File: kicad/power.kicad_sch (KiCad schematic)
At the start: 31 parts, among them J101 24VDC IN, U101 LMR16006YQ5, U102 AMS1117-3.3

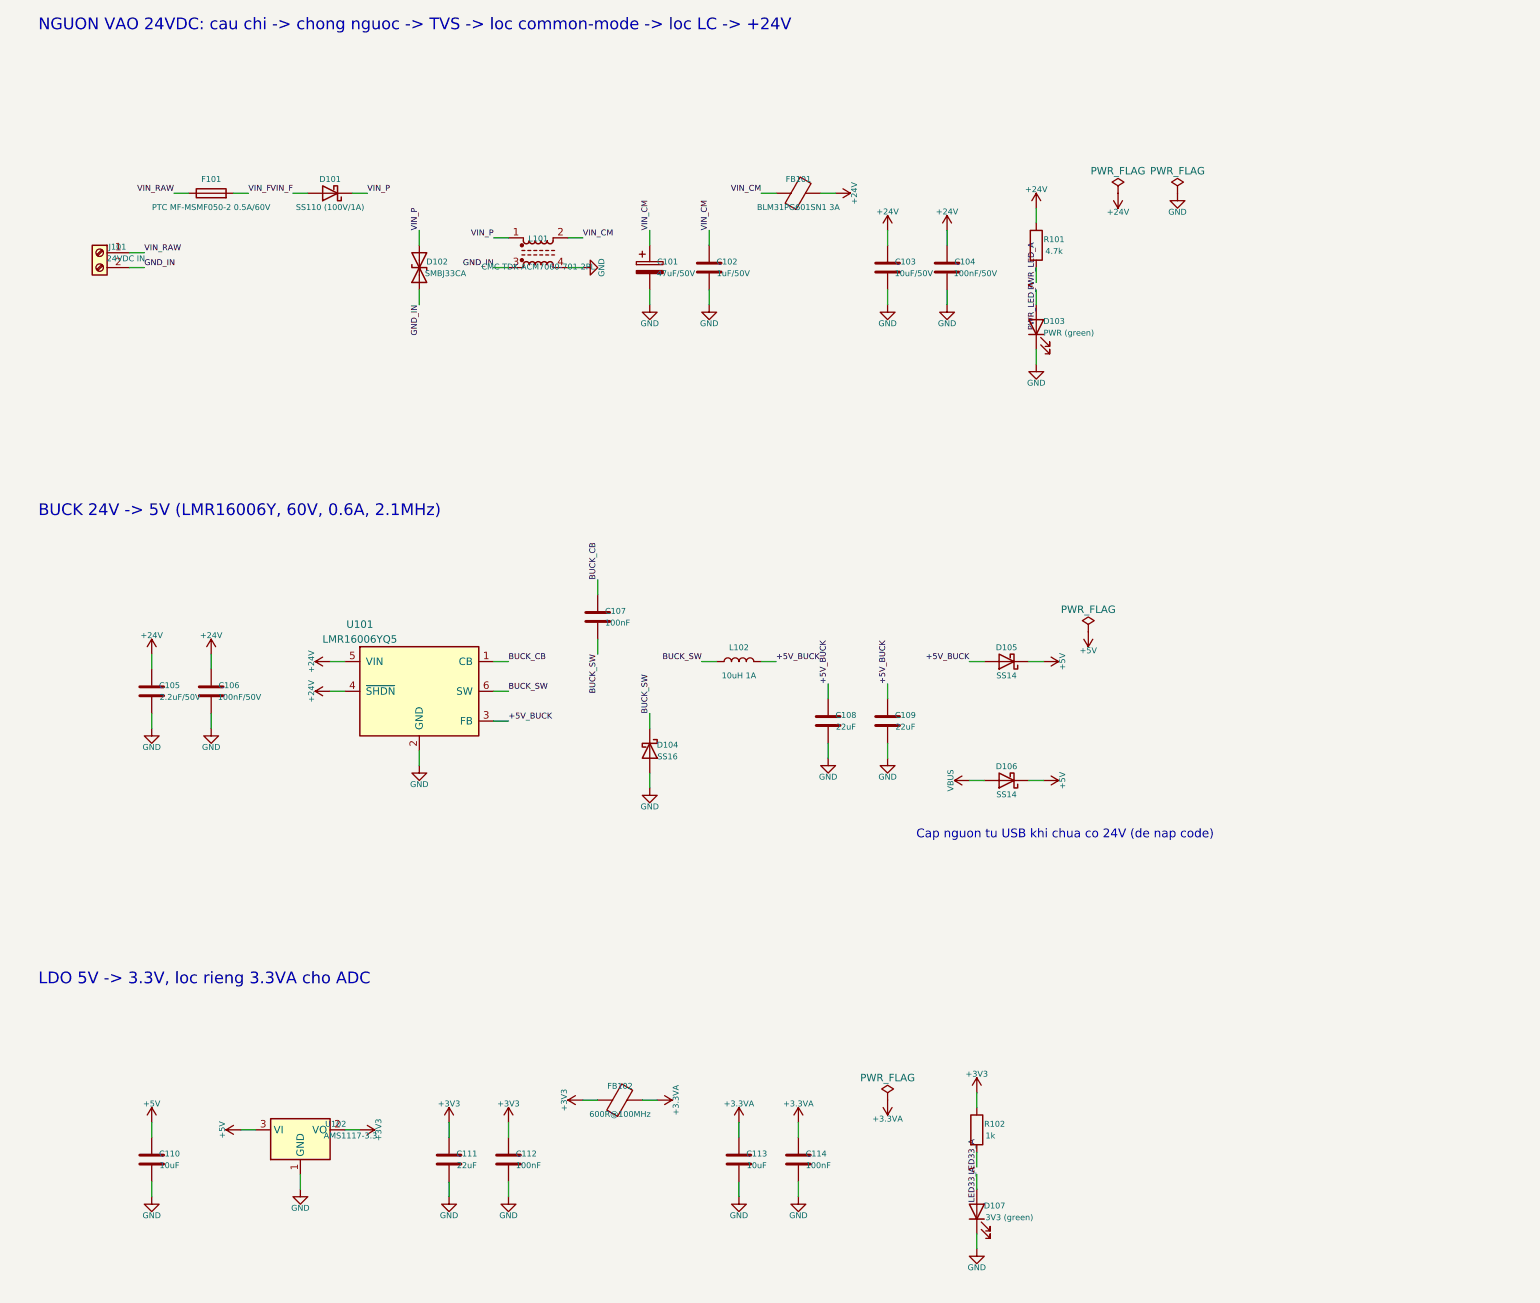
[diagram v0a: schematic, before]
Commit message: - bỏ các mạch 0-10v, RS485 RTU
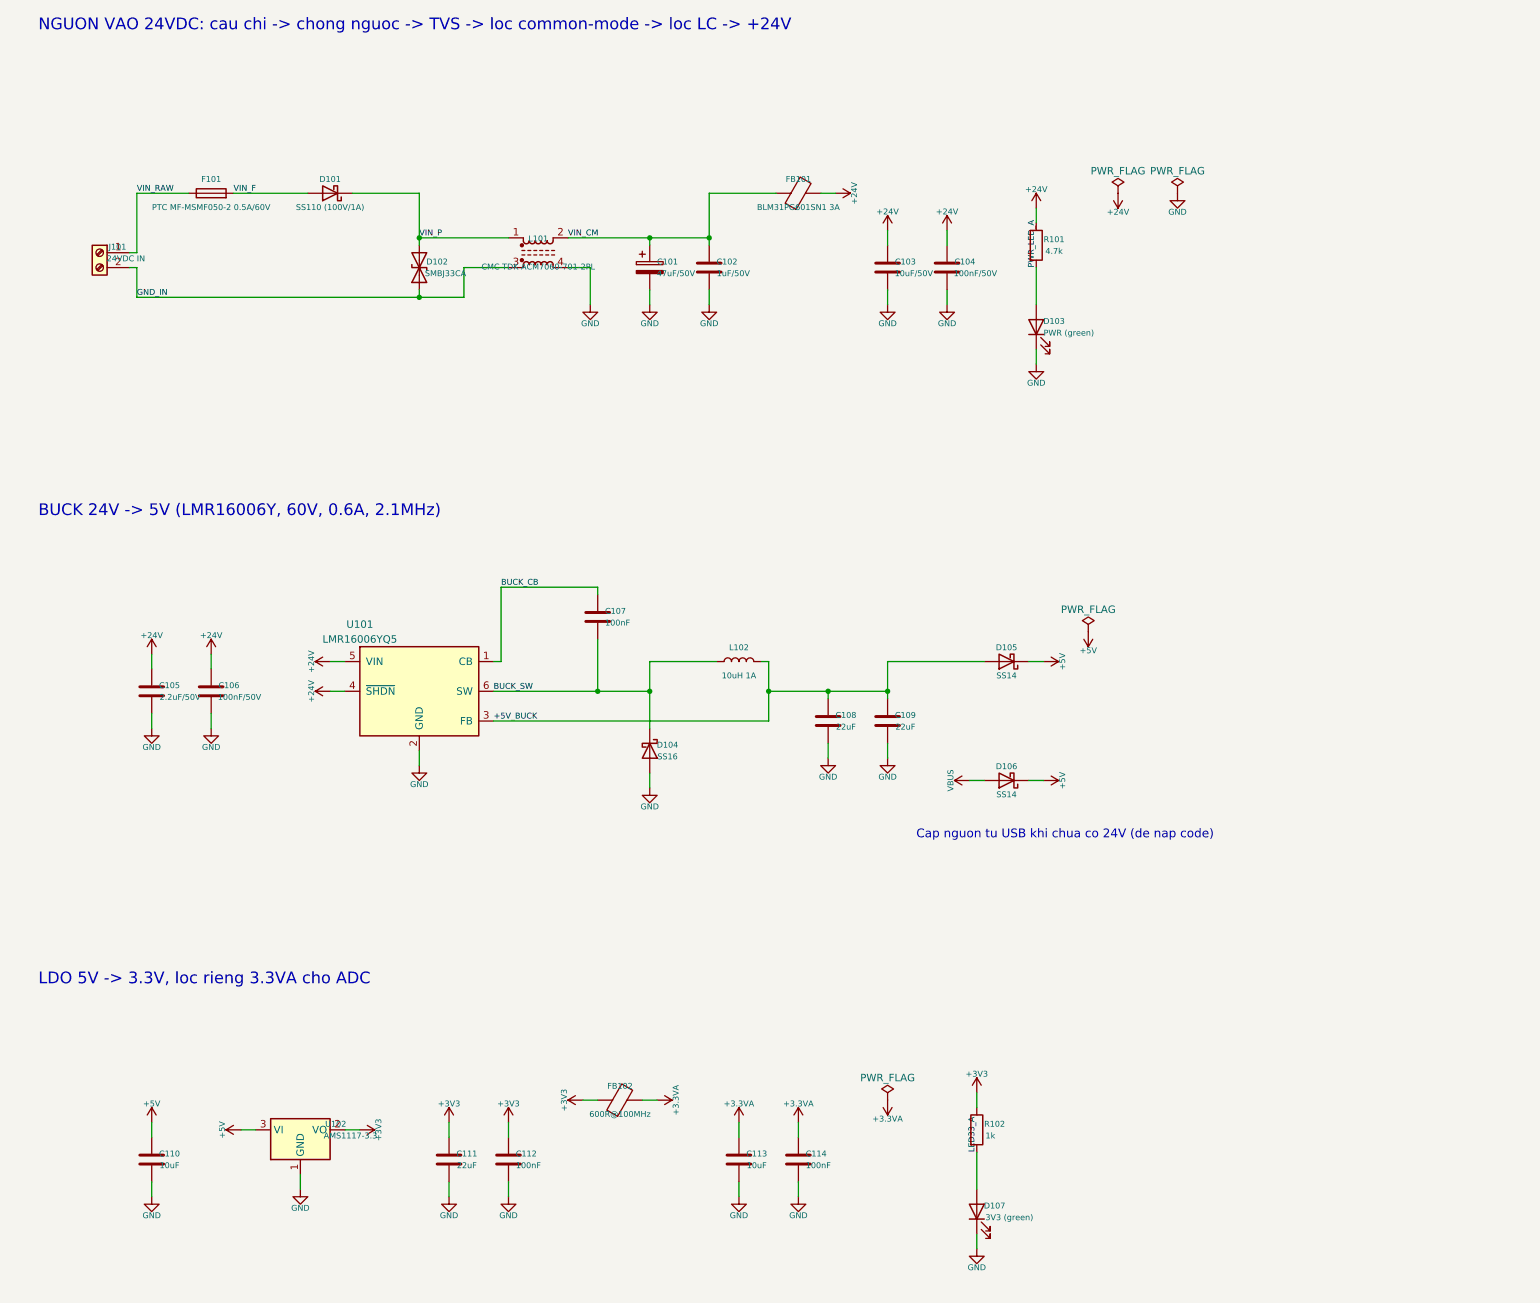
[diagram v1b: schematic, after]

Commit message: - bỏ các cầu chì thêm mô tả cho từng linh kiên
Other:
- note added: "BUCK 24V → 5V (LMR16006Y, 0.6A, f_sw = 2.1MHz)"
- note added: "C101 47µF tụ hóa: dự trữ; ESR dập dao động LC khi cắm nóng. C102 1µF gốm: lọc cao tần."
- note added: "C105 2.2µF/50V + C106 100nF: tụ ngõ vào cấp dòng xung cho khóa đóng cắt, đặt sát VIN–GND."
- note added: "C107 100nF: tụ bootstrap lái MOSFET phía cao (datasheet)."
- note added: "C108, C109 22µF: gợn áp ΔV ≈ ΔI/(8·f·C) = 0.19/(8 × 2.1MHz × 44µF) ≈ 0.26mV."
- note added: "C110 10µF vào; C111 22µF ra (AMS1117 cần ≥ 22µF để ổn định); C112 100nF lọc cao tần."
- note added: "Cầu chì → chống ngược → TVS → lọc common-mode → lọc LC → +24V cho toàn board."
- note added: "D101 SS110 (Schottky 100V): chống cấp ngược cực. Sụt ≈ 0.5V → P ≈ 0.5V × 0.35A ≈ 0.18W."
- note added: "D102 TVS SMBJ33CA: kẹp xung sét/ESD. V_standoff 33V > 28.8V (24V+20%); V_clamp ≈ 53V < 60V (Vin max U101)."
- note added: "D104 SS16 (60V/1A): diode thả trôi, dẫn dòng cuộn cảm khi khóa ngắt."
- note added: "D105, D106 SS14: OR nguồn – lấy 5V từ buck hoặc USB (nạp code khi chưa có 24V), chặn dòng chảy ngược."
- note added: "F101 PTC 0.5A/60V: tự ngắt khi chập/quá tải, tự phục hồi. I_hold > tải ≈ 0.1A (buck) + 0.25A (cảm biến) = 0.35A."
- note added: "FB101 + C103 10µF + C104 100nF: lọc LC thông thấp, chặn nhiễu 2.1MHz của buck dội ngược ra dây nguồn."
- note added: "FB102 (600Ω@100MHz) + C113 + C114: tách +3.3VA sạch cho VDDA, REF3030."
- note added: "Hạ áp hiệu suất ~85%; D = Vout/Vin = 5/24 ≈ 0.21."
- note added: "KHỐI VÀO 24VDC – BẢO VỆ & LỌC NHIỄU"
- note added: "L101 cuộn lọc common-mode: chặn nhiễu đồng pha trên cả 2 dây nguồn (cáp dài, biến tần)."
- note added: "L102 10µH: ΔI = (Vin−Vout)·D/(L·f) = 19V × 0.21/(10µH × 2.1MHz) ≈ 0.19A (≈ 30% I_out). I_sat ≥ 0.6 + ΔI/2 ≈ 0.7A."
- note added: "LDO 5V → 3.3V (AMS1117-3.3)"
- note added: "LED 3.3V: I = (3.3V − 2.0V)/1kΩ ≈ 1.3mA."
- note added: "LED nguồn: I = (24V − 2V)/4.7kΩ ≈ 4.7mA; P_R = 22²/4.7k ≈ 0.1W → R 1206."
- note added: "Tải 3.3V ≈ 260–300mA: STM32 ~100mA + W5500 ~130mA + CH340 + LED."
- note added: "Vin ≈ 4.65V ≥ 3.3V + 1.1V (dropout). P = (4.65 − 3.3) × 0.3A ≈ 0.4W → SOT-223 chịu được."
- note added: "~SHDN nối VIN → luôn chạy. FB nối thẳng ngõ ra (bản 5V cố định, không cần cầu chia)."
